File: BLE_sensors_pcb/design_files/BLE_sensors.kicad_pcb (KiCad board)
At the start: 4 copper layers, 38.2 x 25.1 mm, 49 parts, among them J1 Conn_ARM_SWD_TagConnect_TC203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, J2 Conn_01x02, J3 USB_C_Receptacle, U1 BME280, U2 LSM303AHTR, U3 TPS63031DSK, U4 ME54BS01, U5 MCP73871, U7 MCP2221AxST

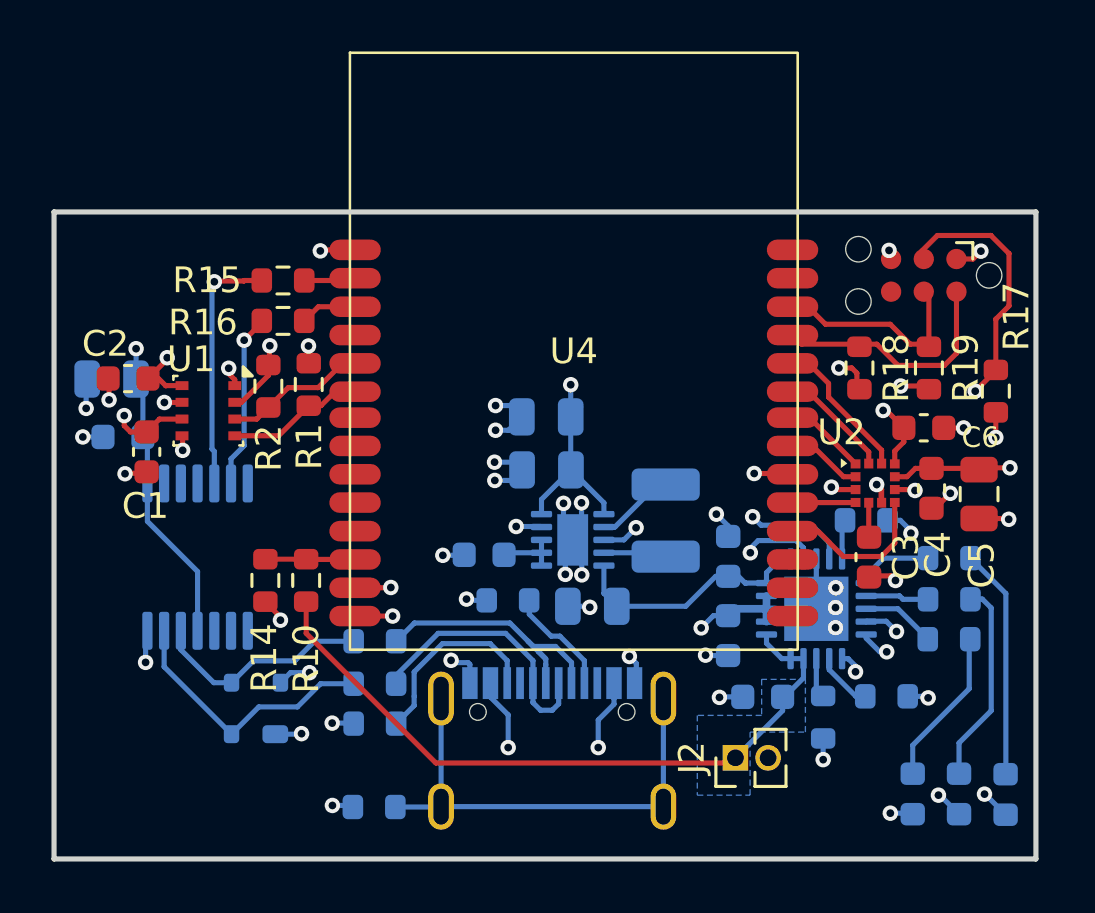
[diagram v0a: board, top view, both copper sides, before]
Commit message: Added a capasitor to me54bs01 pwr supply and added gerbers and schematic
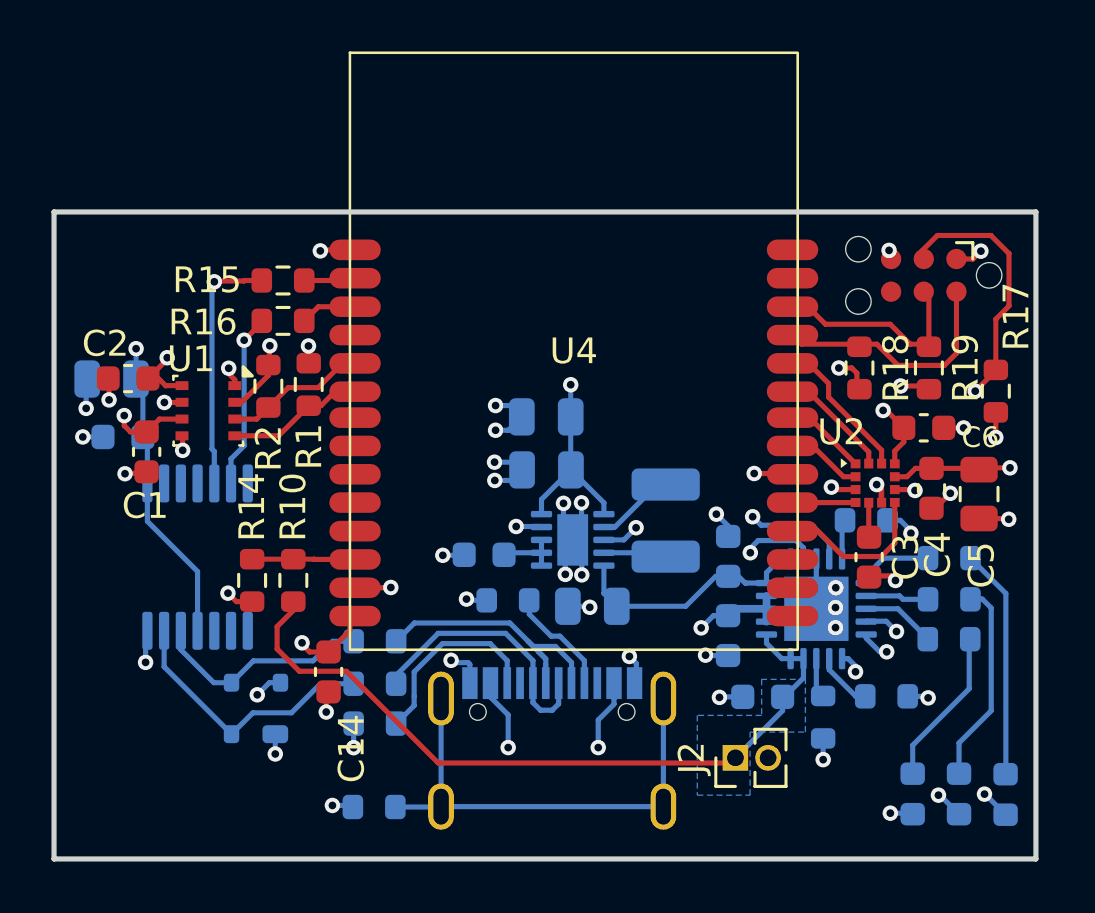
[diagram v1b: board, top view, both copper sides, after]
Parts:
- added C14: 0.1u, Capacitor_SMD:C_0603_1608Metric, F.Cu at (131.8, 85.7)
- moved R14 0.51 mm to (128.8, 82.2)
- moved R10 0.50 mm to (130.4, 82.2)
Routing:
- net +V_bat: track 27.1 -> 28.8 mm
- net +3V3: track 43.0 -> 44.4 mm
- net GND: track 50.2 -> 51.0 mm, vias 49 -> 50
- net Net-(U4-P1.04/AIN0): track 3.49 -> 4.00 mm
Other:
- board text removed: "0"
- board text removed: "0 mm"
- board text removed: "0,01 mm"
- board text removed: "0,02"
- board text removed: "0,035 mm"
- board text removed: "0,1 mm"
- board text removed: "1"
- board text removed: "1,24 mm"
- board text removed: "3,3"
- board text removed: "4,5"
- board text removed: "B.Cu"
- board text removed: "B.Mask"
- board text removed: "B.Paste"
- board text removed: "B.Silkscreen"
- board text removed: "Bottom Silk Screen"
- board text removed: "Bottom Solder Mask"
- board text removed: "Bottom Solder Paste"
- board text removed: "Color"
- board text removed: "Dielectric"
- board text removed: "Epsilon R"
- board text removed: "F.Cu"
- board text removed: "F.Mask"
- board text removed: "F.Paste"
- board text removed: "F.Silkscreen"
- board text removed: "FR4"
- board text removed: "In1.Cu"
- board text removed: "In2.Cu"
- board text removed: "Layer Name"
- board text removed: "Loss Tangent"
- board text removed: "Material"
- board text removed: "Not specified"
- board text removed: "Thickness (mm)"
- board text removed: "Top Silk Screen"
- board text removed: "Top Solder Mask"
- board text removed: "Top Solder Paste"
- board text removed: "Type"
- board text removed: "copper"
- board text removed: "core"
- board text removed: "prepreg"

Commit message: fixed spi
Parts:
- added D5: LED, LED_SMD:LED_0603_1608Metric, F.Cu at (123.8, 90.5)
- added R20: 470R, Resistor_SMD:R_0603_1608Metric, F.Cu at (123.8, 87.2)
- added R21: 10k, Resistor_SMD:R_0603_1608Metric, F.Cu at (151.6, 78.2)
- moved U2 1.05 mm to (154.1, 78.3)
- moved C4 1.00 mm to (156.2, 78.6)
- moved C5 0.94 mm to (158.0, 78.8)
- moved C3 0.75 mm to (152.8, 80.5), turned to 180 degrees
- moved C6 0.53 mm to (155.4, 76.2)
- moved R18 0.50 mm to (152.9, 73.9)
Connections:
- net /SDI renamed /MISO
- U2 pad 2: /CS -> GND
- U4 pad 21: /CS -> Net-(U4-P2.09)
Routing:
- net /CS: track 2.94 -> 0.00 mm
- net /INT_MAG/DRDY: track 6.18 -> 8.64 mm
- net Net-(U4-P2.09): track 0.00 -> 1.99 mm
- net /SPC: track 3.19 -> 5.16 mm
- net +3V3: track 44.4 -> 46.3 mm, vias 13 -> 14
- net Net-(D5-A): track 0.00 -> 1.65 mm
- net GND: track 51.0 -> 52.4 mm, vias 50 -> 51
- net /MISO: track 2.48 -> 3.58 mm
- net /INT1_XL: track 4.38 -> 5.43 mm
- net /INT2_XL: track 5.69 -> 6.42 mm
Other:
- board size 38.2 x 25.1 mm -> 38.3 x 25.1 mm

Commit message: Added pdf
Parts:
- removed D5: LED, LED_SMD:LED_0603_1608Metric
- removed R20: 470R, Resistor_SMD:R_0603_1608Metric
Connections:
- net Net-(U4-P2.09) renamed /MOSI
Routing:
- net Net-(D5-A): track 1.65 -> 0.00 mm
- net GND: track 52.4 -> 51.3 mm, vias 51 -> 50
- net +3V3: track 46.3 -> 45.2 mm, vias 14 -> 13
